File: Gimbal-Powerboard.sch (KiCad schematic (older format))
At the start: 108 parts, among them Q1 Q_PMOS_DGS, Q2 Q_PMOS_DGS, Q3 R6020ENJSMD, Q4 R6020ENJSMD, Q5 R6020ENJSMD, Q6 R6020ENJSMD, Q7 R6020ENJSMD, Q8 R6020ENJSMD, U1 DRV8301, U2 NUP4201MR6, U3 LAUNCHXL-F28069M_Launchpad_J1, U4 MAX3232, U5 Molex_SL-3, U6 Molex_SL-5

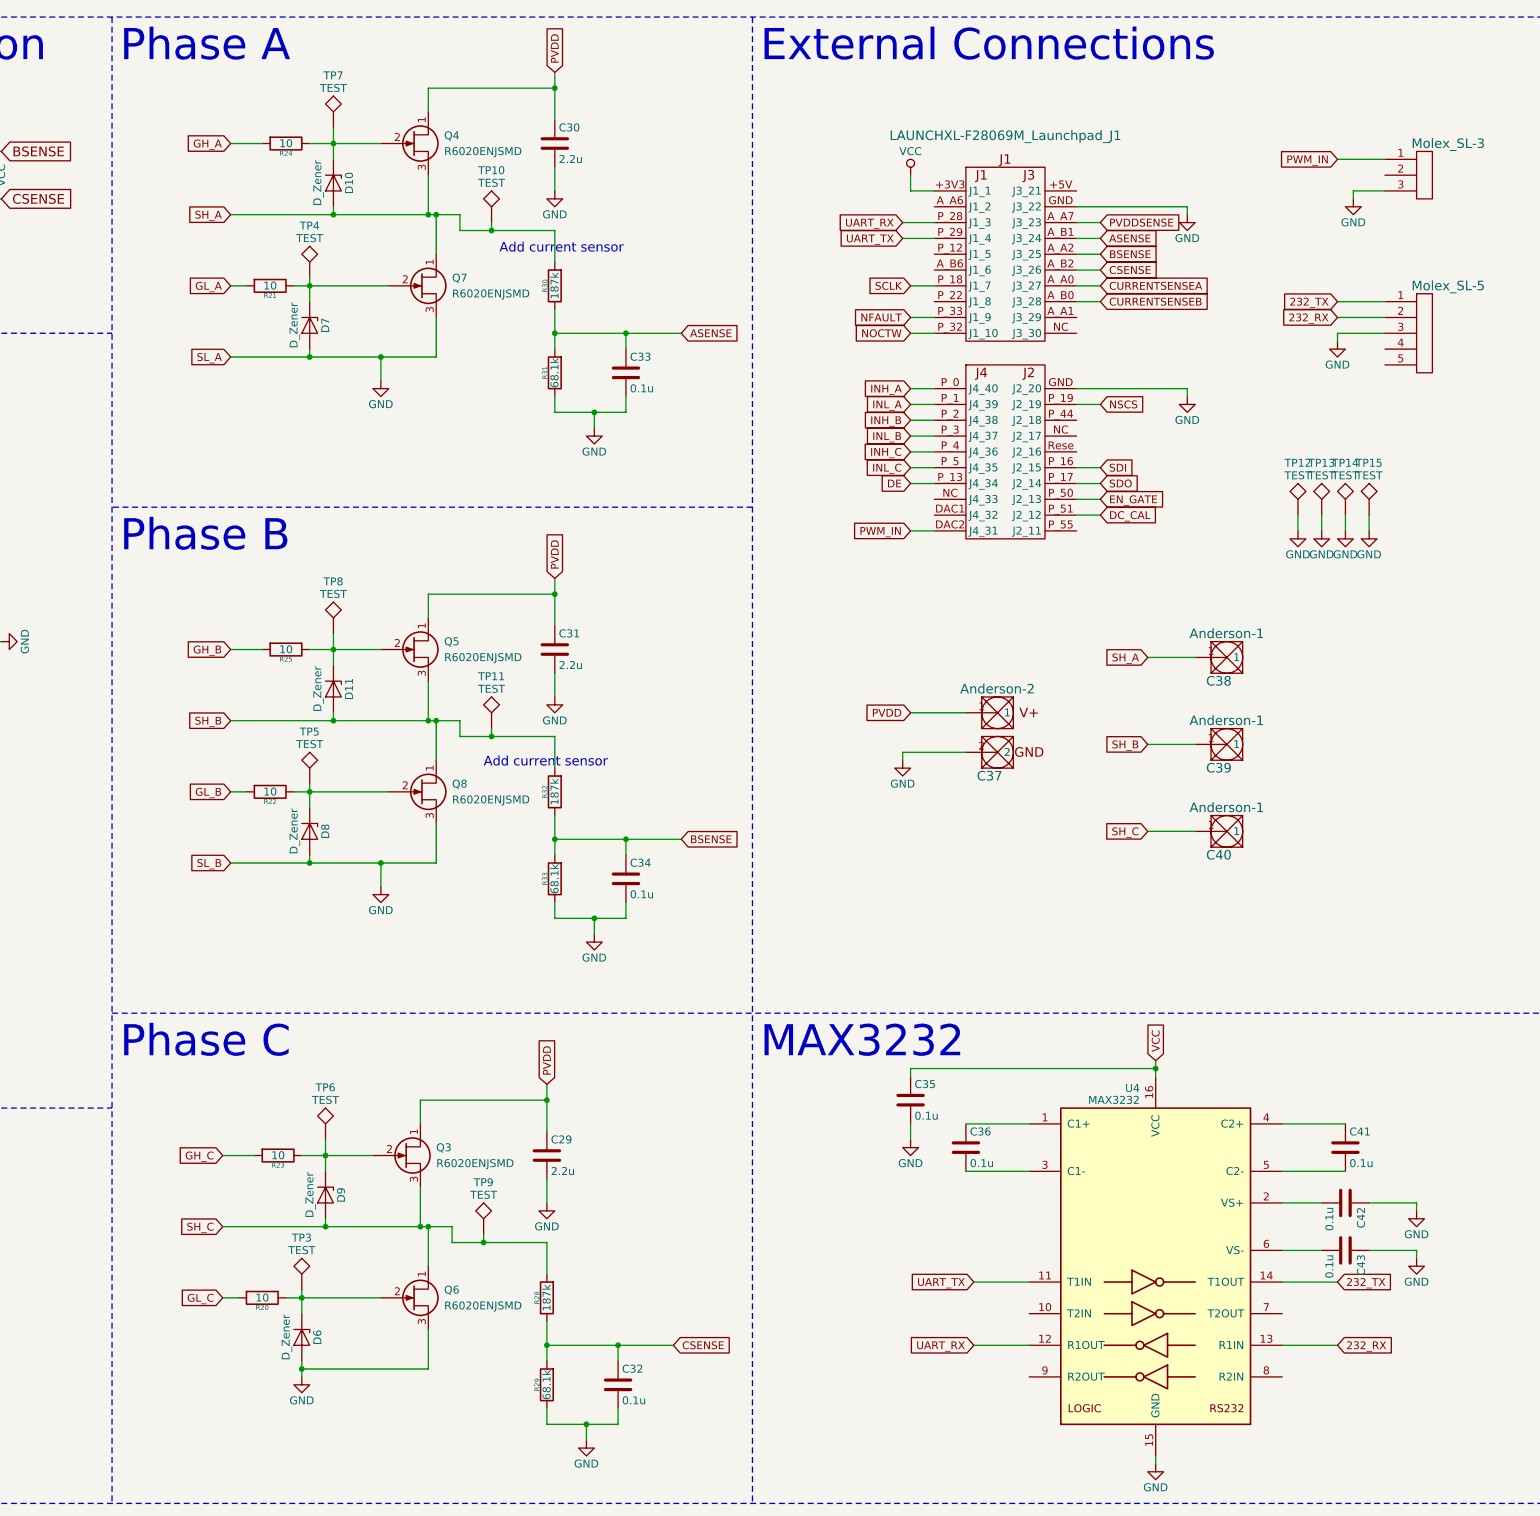
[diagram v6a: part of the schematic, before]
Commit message: Added current sensor
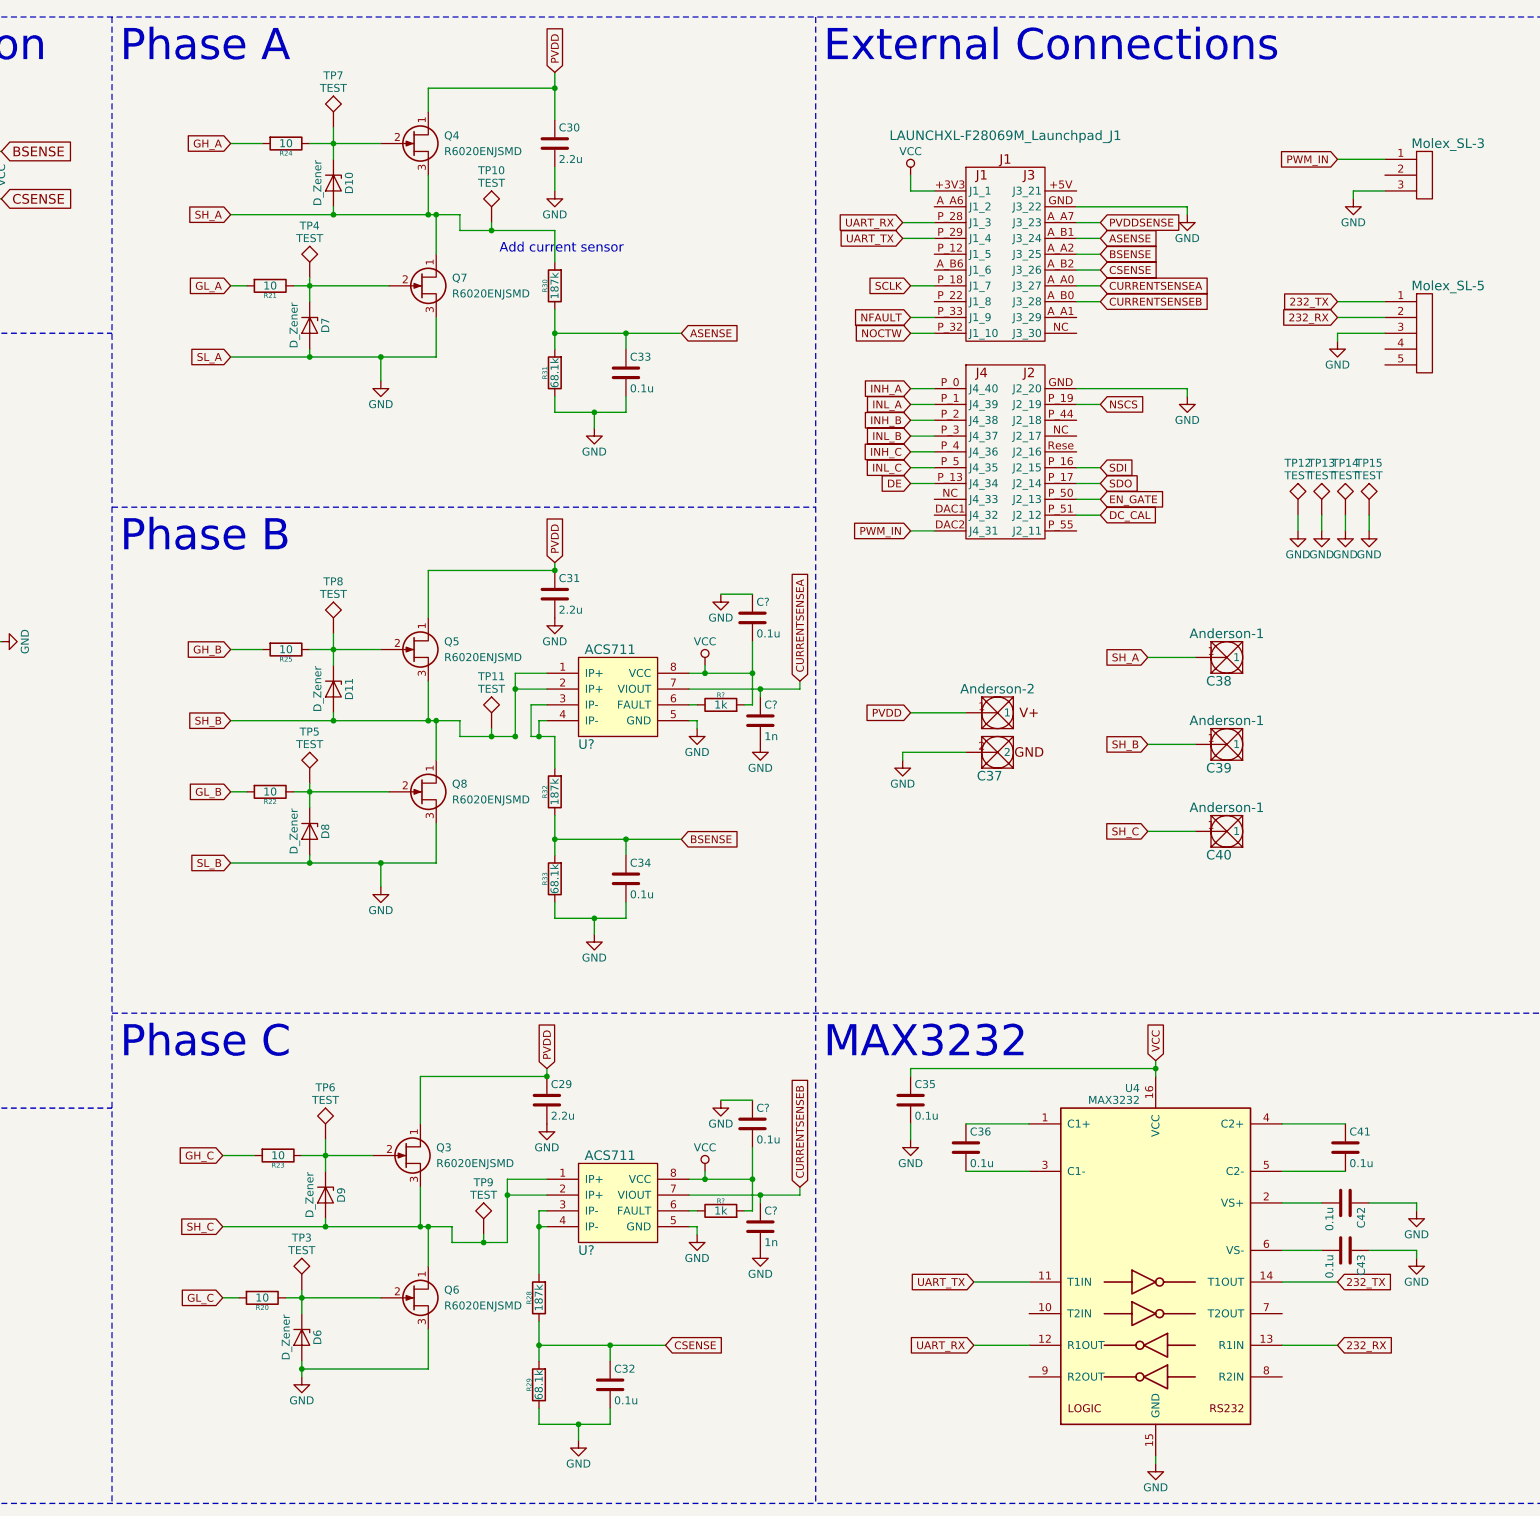
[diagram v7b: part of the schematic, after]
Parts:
- added C? (x2): 0.1u, Capacitors_SMD:C_0805_HandSoldering, symbol C
- added C? (x2): 1n, Capacitors_SMD:C_0805_HandSoldering, symbol C
- added R? (x2): 1k, Resistors_SMD:R_0805_HandSoldering, symbol R
- added U? (x2): ACS711, symbol ACS711
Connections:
- net CURRENTSENSEA: now also C?.1, U?.7 (VIOUT)
- net CURRENTSENSEB: now also C?.1, U?.7 (VIOUT)
- net GND: now also C?.1, C?.1, C?.2, C?.2, U?.5 (GND), U?.5 (GND)
- net SH_B: now also U?.1 (IP+), U?.2 (IP+); no longer R32.2
- net SH_C: now also U?.1 (IP+), U?.2 (IP+); no longer R28.2
- net VCC: now also C?.2, C?.2, R?.2, R?.2, U?.8 (VCC), U?.8 (VCC)
- new net: R32.2, U?.3 (IP-), U?.4 (IP-)
- new net: R28.2, U?.3 (IP-), U?.4 (IP-)
- new net: R?.1, U?.6 (FAULT) (x2)
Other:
- moved on the sheet: C29, C31, C32, R28, R29

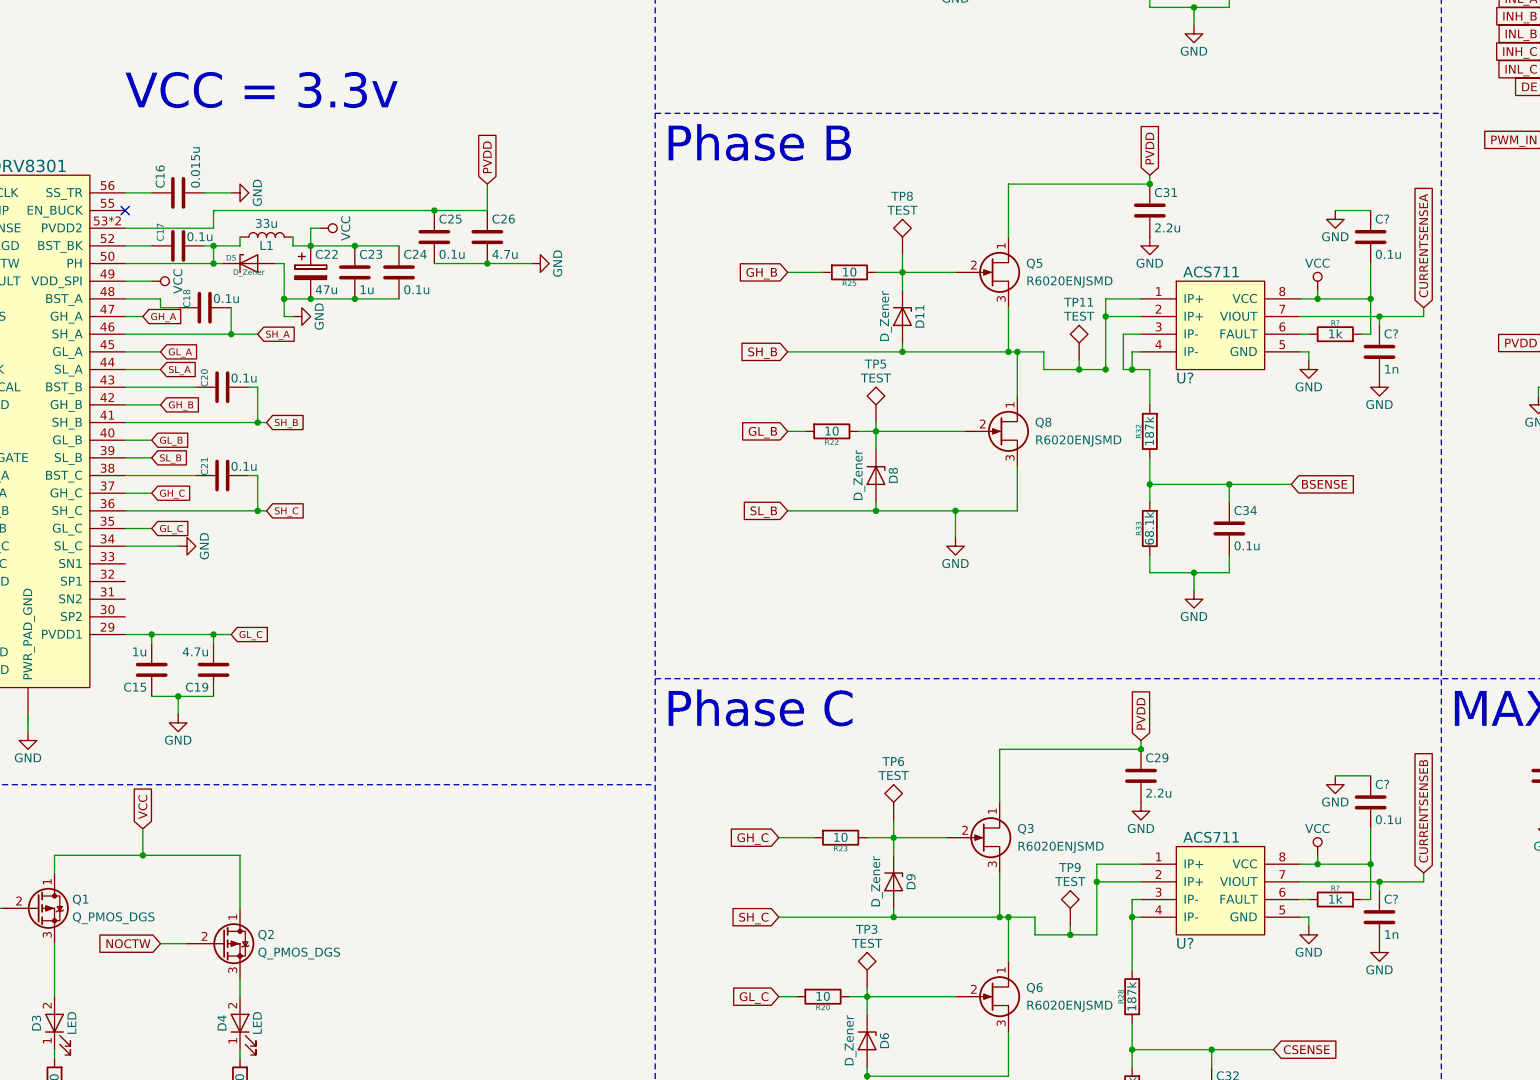
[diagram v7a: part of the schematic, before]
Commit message: Added netlist, updated drv8301 implementation
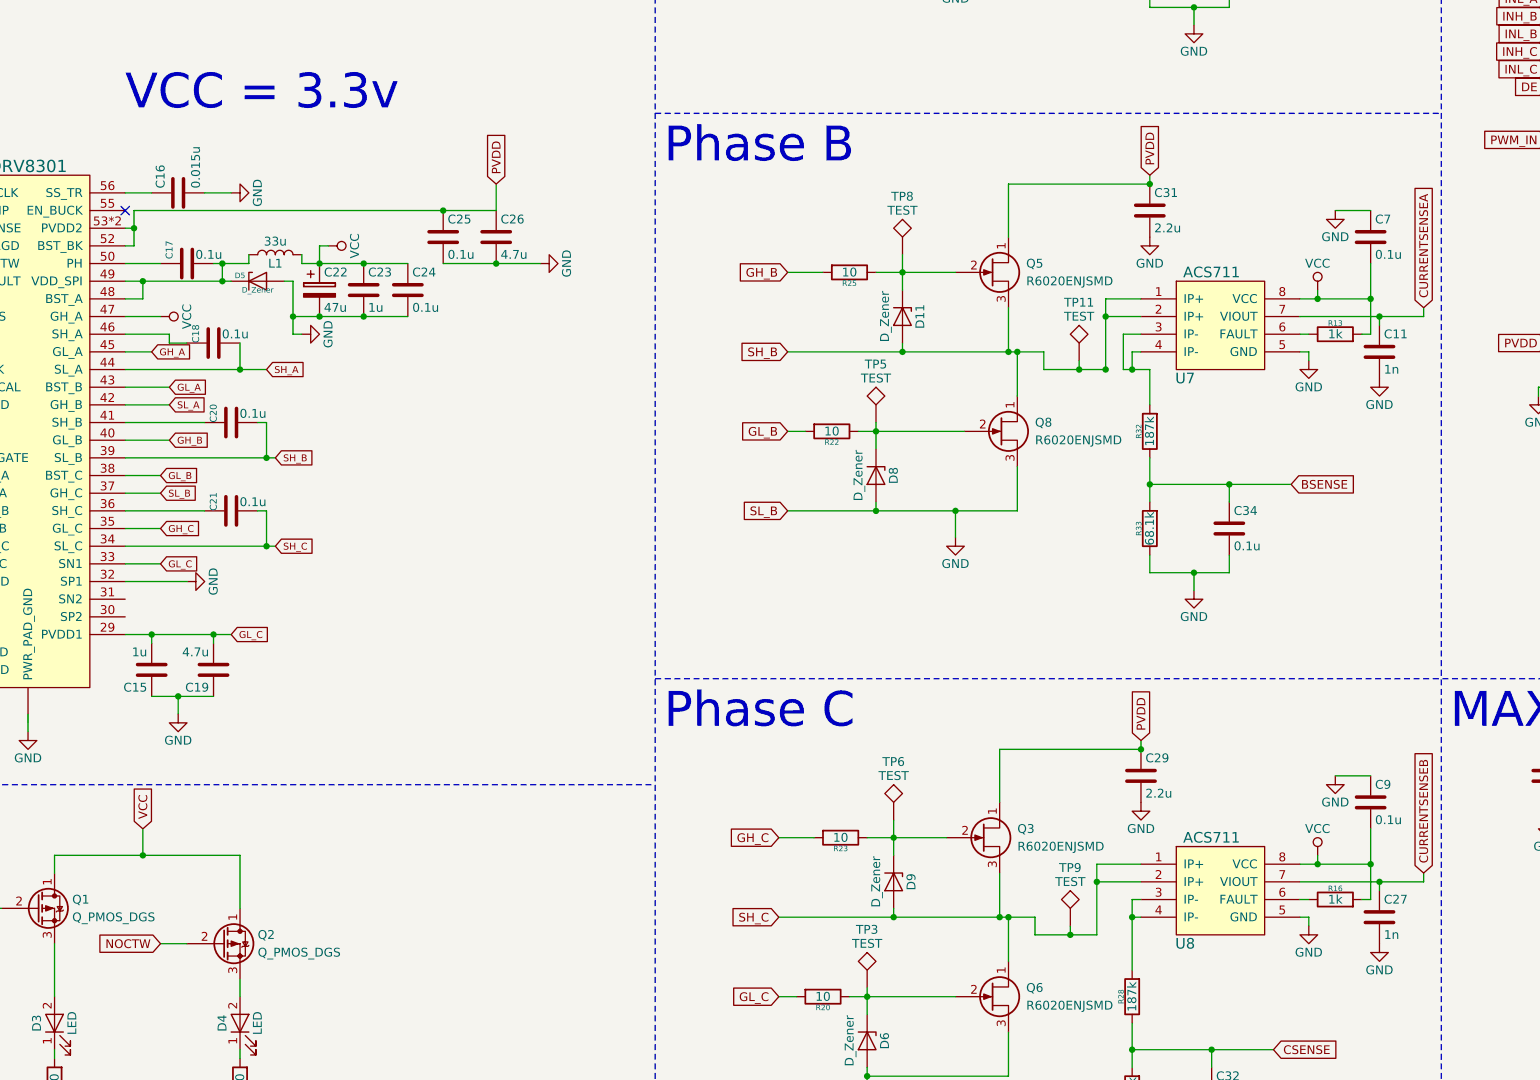
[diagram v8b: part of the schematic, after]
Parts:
- C37: footprint MRDT-Connectors:Anderson_2_Horisontal_Side-by-Side -> MRDT_Connectors:Anderson_2_Horisontal_Side_by_Side
- C38, C39, C40: footprint MRDT-Connectors:Anderson_1_Horisontal -> MRDT_Connectors:Anderson_1_Horisontal
- L1: footprint MRDT-Passives:DR74-330-R -> MRDT_Passives:DR74_330_R
- Q3, Q4, Q5, Q6, Q7, Q8: footprint MRDT-Actives:Rohm_R6020ENJ_N-Channel_MOSFET -> MRDT_Actives:Rohm_R6020ENJ_N_Channel_MOSFET
- U1: footprint MRDT-ICs:DRV8301 -> MRDT_ICs:DRV8301
- U2: footprint MRDT-ICs:NUP4201MR6 -> MRDT_ICs:NUP4201MR6
- U3: footprint MRDT-Shields:LAUNCHXL-F28069M_Launchpad_J1 -> MRDT_Shields:LAUNCHXL_F28069M_Launchpad_J1
- U4: footprint MRDT-ICs:SOIC-16_3.9x9.9mm_Pitch1.27mm -> MRDT_ICs:SOIC-16_3.9x9.9mm_Pitch1.27mm
- U5: footprint MRDT-Connectors:MOLEX_SL_3 -> MRDT_Connectors:MOLEX_SL_3
- U6: footprint MRDT-Connectors:MOLEX_SL_5 -> MRDT_Connectors:MOLEX_SL_5
- U7, U8: renamed from U?; footprint (none) -> ACS711:SOIC127P600X175-8N
- gave numbers to parts that had none: 6
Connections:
- net GH_A: now also U1.45 (GL_A); no longer U1.47 (GH_A)
- net GH_B: now also U1.40 (GL_B); no longer U1.42 (GH_B)
- net GH_C: now also U1.35 (GL_C); no longer U1.37 (GH_C)
- net GL_A: now also U1.43 (BST_B); no longer U1.45 (GL_A)
- net GL_B: now also U1.38 (BST_C); no longer U1.40 (GL_B)
- net GL_C: now also U1.33 (SN1); no longer U1.35 (GL_C)
- net GND: now also U1.32 (SP1), U1.37 (GH_C), U1.42 (GH_B); no longer U1.34 (SL_C), U1.39 (SL_B), U1.44 (SL_A)
- net PVDD: now also U1.52 (BST_BK)
- net SH_A: now also U1.44 (SL_A); no longer U1.46 (SH_A)
- net SH_B: now also U1.39 (SL_B); no longer U1.41 (SH_B)
- net SH_C: now also U1.34 (SL_C); no longer U1.36 (SH_C)
- net VCC: now also U1.47 (GH_A); no longer U1.49 (VDD_SPI)
- net at C21.1: now also U1.36 (SH_C); no longer U1.38 (BST_C)
- net at C20.1: now also U1.41 (SH_B); no longer U1.43 (BST_B)
- net at C18.1: now also U1.46 (SH_A); no longer U1.48 (BST_A)
- net at C17.2, D5.1 (K), L1.1: now also U1.48 (BST_A), U1.49 (VDD_SPI); no longer U1.50 (PH)
- net at C17.1: now also U1.50 (PH); no longer U1.52 (BST_BK)
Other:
- moved on the sheet: C17, C18, C20, C21, C22, C23, C24, C25, C26, D5, L1
